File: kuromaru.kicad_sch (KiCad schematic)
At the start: 113 parts, among them J1 USB_C_Receptacle_USB2.0, J102 Serial, J5 Conn_01x02, SW1 SW_Push, SW101 SW_Push, SW102 SW_Push, SW103 SW_Push, SW104 SW_Push, SW105 SW_Push, SW106 SW_Push, SW107 SW_Push, SW108 SW_Push, SW109 SW_Push, SW110 SW_SPST, SW112 SW_Push, SW113 SW_Push, SW114 SW_Push, SW115 SW_Push, SW116 SW_Push, SW117 SW_Push, SW118 SW_Push, SW119 SW_Push, SW2 SW_Push, U1 RP2040, U2 GD25Q80CEIGR, U3 XC6210B332MR-G, Y1 Crystal_GND24

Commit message: Before diodeless design
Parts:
- removed D101, D102, D103, D104, D105, D106, D107, D108, D109, D110, D111, D112, D113, D114, D115, D116, D117: D, local-libraries:D_1206_handsolder_reversible, symbol Device:D
- removed SW101, SW102, SW103, SW104, SW105, SW106, SW107, SW108, SW109, SW112, SW113, SW114, SW115, SW116, SW117, SW118, SW119: SW_Push, local-libraries:SW_MX_choc, symbol Switch:SW_Push
- added C?: C, Capacitor_SMD:C_1206_3216Metric_Pad1.42x1.75mm_HandSolder, symbol Device:C
- added R?: R, Resistor_SMD:R_1206_3216Metric_Pad1.42x1.75mm_HandSolder, symbol Device:R
- SW1, SW2: symbol Switch:SW_Push -> delay_SW_MX_RGB:SW_Push_SK6812
- SW11, SW12, SW13, SW14, SW15, SW21, SW22, SW23, SW24, SW25, SW31, SW32, SW33, SW34, SW35, SW41, SW42: renamed from SW?; value SW_Push -> SW_Push_SK6812; symbol Switch:SW_Push -> delay_SW_MX_RGB:SW_Push_SK6812
- gave numbers to parts that had none: 5
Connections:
- net Din: now also R?.1
- net GND: no longer SW1.1, SW2.1
- net Gnd: now also SW11.3 (GND), SW11.5, SW12.3 (GND), SW12.5, SW13.3 (GND), SW13.5, SW14.3 (GND), SW14.5, SW15.3 (GND), SW15.5, SW21.3 (GND), SW21.5, SW22.3 (GND), SW22.5, SW23.3 (GND), SW23.5, SW24.3 (GND), SW24.5, SW25.3 (GND), SW25.5, SW31.3 (GND), SW31.5, SW32.3 (GND), SW32.5, SW33.3 (GND), SW33.5, SW34.3 (GND), SW34.5, SW35.3 (GND), SW35.5, SW41.3 (GND), SW41.5, SW42.3 (GND), SW42.5, C?.2; no longer SW11.1, SW12.1, SW13.1, SW14.1, SW15.1, SW21.1, SW22.1, SW23.1, SW24.1, SW25.1, SW31.1, SW32.1, SW33.1, SW34.1, SW35.1, SW41.1, SW42.1
- net Rst_l: no longer SW1.2
- net Vcc: now also SW11.1 (VDD), SW12.1 (VDD), SW13.1 (VDD), SW14.1 (VDD), SW15.1 (VDD), SW21.1 (VDD), SW22.1 (VDD), SW23.1 (VDD), SW24.1 (VDD), SW25.1 (VDD), SW31.1 (VDD), SW32.1 (VDD), SW33.1 (VDD), SW34.1 (VDD), SW35.1 (VDD), SW41.1 (VDD), SW42.1 (VDD), C?.1
- net switch11: now also SW11.6; no longer SW11.2, SW21.2, SW31.2
- net switch12: now also SW12.6; no longer SW12.2, SW22.2, SW32.2
- net switch13: now also SW13.6; no longer SW13.2, SW23.2, SW33.2
- net switch14: now also SW14.6; no longer SW14.2, SW24.2, SW34.2, SW41.2
- net switch15: now also SW15.6; no longer SW15.2, SW25.2, SW35.2, SW42.2
- net switch21: now also SW21.6
- net switch22: now also SW22.6
- net switch23: now also SW23.6
- net switch24: now also SW24.6
- net switch25: now also SW25.6
- net at J5.2 (Pin_2), R3.1: no longer SW2.2
- new net switch31: SW31.6
- new net switch32: SW32.6
- new net switch33: SW33.6
- new net switch34: SW34.6
- new net switch35: SW35.6
- new net switch41: SW41.6
- new net switch42: SW42.6
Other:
- note added: "RGB backlight"
- note added: "Switches & RGB Backlight"
- note removed: "Diodes and switches - plate"
- note removed: "Diodes and switches - thumb cluster"
- note removed: "RGB backlight - plate"

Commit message: Update to diodeless
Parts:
- removed C? (x2): C, Capacitor_SMD:C_1206_3216Metric_Pad1.42x1.75mm_HandSolder, symbol Device:C
- removed D11, D12, D13, D14, D15, D? (x12): SK6812MINI, libs2:YS-SK6812MINI-E_REVERSE, symbol LED:SK6812MINI
- removed JP111, JP112: Jumper_2_Open, local-libraries:SolderJumper-2_P1.3mm_Open_RoundedPad1.0x1.5mm, symbol Jumper:Jumper_2_Open
- removed R?: R, Resistor_SMD:R_1206_3216Metric_Pad1.42x1.75mm_HandSolder, symbol Device:R
- J102: footprint local-libraries:Jack_3.5mm_PJ320E_Horizontal_custom -> keebio:TRRS-PJ-320A-no-Fmask
- SW11: renamed from SW15; footprint local-libraries:SW_MX_choc -> local-libraries:delay_SW_MX_RGB
- SW12: renamed from SW25; footprint local-libraries:SW_MX_choc -> local-libraries:delay_SW_MX_RGB
- SW13: renamed from SW35; footprint local-libraries:SW_MX_choc -> local-libraries:delay_SW_MX_RGB
- SW14: renamed from SW42; footprint local-libraries:SW_MX_choc -> local-libraries:delay_SW_MX_RGB
- SW21: renamed from SW14; footprint local-libraries:SW_MX_choc -> local-libraries:delay_SW_MX_RGB
- SW22: renamed from SW24; footprint local-libraries:SW_MX_choc -> local-libraries:delay_SW_MX_RGB
- SW23: renamed from SW34; footprint local-libraries:SW_MX_choc -> local-libraries:delay_SW_MX_RGB
- SW24: renamed from SW41; footprint local-libraries:SW_MX_choc -> local-libraries:delay_SW_MX_RGB
- SW31: renamed from SW13; footprint local-libraries:SW_MX_choc -> local-libraries:delay_SW_MX_RGB
- SW32: renamed from SW23; footprint local-libraries:SW_MX_choc -> local-libraries:delay_SW_MX_RGB
- SW33: footprint local-libraries:SW_MX_choc -> local-libraries:delay_SW_MX_RGB
- SW41: renamed from SW12; footprint local-libraries:SW_MX_choc -> local-libraries:delay_SW_MX_RGB
- SW42: renamed from SW22; footprint local-libraries:SW_MX_choc -> local-libraries:delay_SW_MX_RGB
- SW43: renamed from SW32; footprint local-libraries:SW_MX_choc -> local-libraries:delay_SW_MX_RGB
- SW51: renamed from SW11; footprint local-libraries:SW_MX_choc -> local-libraries:delay_SW_MX_RGB
- SW52: renamed from SW21; footprint local-libraries:SW_MX_choc -> local-libraries:delay_SW_MX_RGB
- SW53: renamed from SW31; footprint local-libraries:SW_MX_choc -> local-libraries:delay_SW_MX_RGB
- gave numbers to parts that had none: 2
- renumbered SW110 to SW00
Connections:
- net Gnd is gone; now on net GND: C101.2, SW11.3 (GND), SW11.5, SW12.3 (GND), SW12.5, SW13.3 (GND), SW13.5, SW14.3 (GND), SW14.5, SW21.3 (GND), SW21.5, SW22.3 (GND), SW22.5, SW23.3 (GND), SW23.5, SW24.3 (GND), SW24.5, SW31.3 (GND), SW31.5, SW32.3 (GND), SW32.5, SW33.3 (GND), SW33.5, SW41.3 (GND), SW41.5, SW42.3 (GND), SW42.5, SW43.3 (GND), SW43.5, SW51.3 (GND), SW51.5, SW52.3 (GND), SW52.5, SW53.3 (GND), SW53.5
- net Vcc is gone; now on net +5V: C101.1, SW11.1 (VDD), SW12.1 (VDD), SW13.1 (VDD), SW14.1 (VDD), SW21.1 (VDD), SW22.1 (VDD), SW23.1 (VDD), SW24.1 (VDD), SW31.1 (VDD), SW32.1 (VDD), SW33.1 (VDD), SW41.1 (VDD), SW42.1 (VDD), SW43.1 (VDD), SW51.1 (VDD), SW52.1 (VDD), SW53.1 (VDD)
- net switch34 is gone; now on net switch23: SW23.6
- net switch35 is gone; now on net switch13: SW13.6
- net Gnd_l: now also J102.S; no longer J102.R1
- net serial_tx: now also J102.R1; no longer J102.S
- net switch11: now also SW11.6; no longer SW51.6
- net switch12: now also SW12.6; no longer SW41.6
- net switch13: no longer SW31.6
- net switch14: now also SW14.6; no longer SW21.6
- net switch15: no longer SW11.6
- net switch21: now also SW21.6; no longer SW52.6
- net switch22: now also SW22.6; no longer SW42.6
- net switch23: no longer SW32.6
- net switch24: now also SW24.6; no longer SW22.6
- net switch25: no longer SW12.6
- net switch31: now also SW31.6; no longer SW53.6
- net switch32: now also SW32.6; no longer SW43.6
- net switch41: now also SW41.6; no longer SW24.6
- net switch42: now also SW42.6; no longer SW14.6
- net at SW12.2 (DOUT): now also SW53.4 (DIN)
- net at SW12.4 (DIN): now also SW22.2 (DOUT)
- net at SW52.2 (DOUT): now also SW42.4 (DIN)
- net at SW52.4 (DIN): now also SW11.2 (DOUT)
- net at SW41.2 (DOUT): now also SW31.4 (DIN)
- net at SW41.4 (DIN): now also SW51.2 (DOUT)
- net at SW42.2 (DOUT): now also SW32.4 (DIN)
- net at SW24.2 (DOUT): now also SW14.4 (DIN)
- net at SW24.4 (DIN): now also SW13.2 (DOUT)
- net at SW13.4 (DIN): now also SW23.2 (DOUT)
- net at SW22.4 (DIN): now also SW32.2 (DOUT)
- net at SW33.2 (DOUT): now also SW23.4 (DIN)
- net at SW33.4 (DIN): now also SW43.2 (DOUT)
- net at SW43.4 (DIN): now also SW53.2 (DOUT)
- net at SW31.2 (DOUT): now also SW21.4 (DIN)
- net at R102.2: now also SW51.4 (DIN)
- net at SW11.4 (DIN): now also SW21.2 (DOUT)
- new net switch43: SW43.6
- new net switch51: SW51.6
- new net switch52: SW52.6
- new net switch53: SW53.6
- no-connect marks 10 -> 11
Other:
- note removed: "RGB backlight"
- moved on the sheet: C101, R102, SW11, SW12, SW13, SW14, SW21, SW22, SW23, SW24, SW31, SW32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

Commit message: Rework controller, commit before splay
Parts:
- removed SW00: SW_SPST, local-libraries:SW_Push_1P1T_NO_6x6mm_H9.5mm, symbol Switch:SW_SPST
- added R12, R13: 100k, Resistor_SMD:R_0402_1005Metric, symbol Device:R
- added R16, R17: 5.1k, Resistor_SMD:R_0402_1005Metric, symbol Device:R
- added U4: 25LCxxx, Package_SO:SOIC-8_3.9x4.9mm_P1.27mm, symbol Memory_EEPROM:25LCxxx
- C15: renamed from C101; value C -> 1µ; footprint Capacitor_SMD:C_1206_3216Metric_Pad1.42x1.75mm_HandSolder -> Capacitor_SMD:C_0402_1005Metric
- J102: footprint keebio:TRRS-PJ-320A-no-Fmask -> local-libraries:delay_TRRS_PJ_320A
- R15: renamed from R102; value R -> 300; footprint Resistor_SMD:R_1206_3216Metric_Pad1.42x1.75mm_HandSolder -> Resistor_SMD:R_0402_1005Metric
- SW1, SW2: symbol delay_SW_MX_RGB:SW_Push_SK6812 -> Switch:SW_Push
- renumbered SW11 to C1R1, SW12 to C1R2, SW13 to C1R3, SW14 to C1R4, SW21 to C2R1, SW22 to C2R2, SW23 to C2R3, SW24 to C2R4, SW31 to C3R1, SW32 to C3R2, SW33 to C3R3, SW41 to C4R1, SW42 to C4R2, SW43 to C4R3, SW51 to C5R1, SW52 to C5R2, SW53 to C5R3, R101 to R14
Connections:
- net Din is gone; now on net rgb_din: R15.1
- net Gnd_l is gone; now on net GND: J102.S
- net Rst_l is gone; now on net reset: R2.1, U1.26 (RUN/~{RST})
- net hand is gone; now on net hands: R14.1
- net switch42 is gone; now on net switch_c4r2: C4R2.6
- net +3V3: now also C15.1, C1R1.1 (VDD), C1R2.1 (VDD), C1R3.1 (VDD), C1R4.1 (VDD), C2R1.1 (VDD), C2R2.1 (VDD), C2R3.1 (VDD), C2R4.1 (VDD), C3R1.1 (VDD), C3R2.1 (VDD), C3R3.1 (VDD), C4R1.1 (VDD), C4R2.1 (VDD), C4R3.1 (VDD), C5R1.1 (VDD), C5R2.1 (VDD), C5R3.1 (VDD), R12.2, R16.2, R17.2, U4.8 (VCC); no longer J102.T
- net +5V: no longer C15.1, C1R1.1 (VDD), C1R2.1 (VDD), C1R3.1 (VDD), C1R4.1 (VDD), C2R1.1 (VDD), C2R2.1 (VDD), C2R3.1 (VDD), C2R4.1 (VDD), C3R1.1 (VDD), C3R2.1 (VDD), C3R3.1 (VDD), C4R1.1 (VDD), C4R2.1 (VDD), C4R3.1 (VDD), C5R1.1 (VDD), C5R2.1 (VDD), C5R3.1 (VDD)
- net GND: now also R14.2, SW1.1, SW2.1, R13.1, U4.4 (GND)
- net MISO: now also U4.2 (MISO)
- net MOSI: now also U4.5 (MOSI)
- net SCLK: now also R13.2, U4.6 (SCK)
- net VBUS: now also J102.T
- net serial_rx: now also U1.37 (GPIO25); no longer U1.4 (GPIO2)
- net serial_tx: now also U1.36 (GPIO24); no longer U1.3 (GPIO1)
- net at J5.2 (Pin_2), R3.1: now also SW2.2
- net reset: now reaches SW1.2
- net A3 renamed hands
- net D21 renamed EEPROM_CS
- net EEPROM_CS: now also R12.1, U4.1 (~{CS})
- net switch11 renamed switch_c1r1
- net switch_c1r1: now also U1.3 (GPIO1); no longer U1.5 (GPIO3)
- net switch12 renamed switch_c1r2
- net switch_c1r2: now also U1.13 (GPIO10); no longer U1.6 (GPIO4)
- net switch13 renamed switch_c1r3
- net switch_c1r3: now also U1.18 (GPIO15); no longer U1.7 (GPIO5)
- net switch14 renamed switch_c1r4
- net switch_c1r4: now also U1.29 (GPIO18); no longer U1.8 (GPIO6)
- net switch15 renamed switch_c4r2
- removed net switch21: C2R1.6, U1.11 (GPIO8), U1.16 (GPIO13)
- net switch22 renamed switch_c2r2
- net switch_c2r2: no longer U1.17 (GPIO14)
- removed net switch23: C2R3.6, U1.13 (GPIO10), U1.18 (GPIO15)
- net switch24 renamed switch_c2r4
- net switch_c2r4: no longer U1.14 (GPIO11), U1.36 (GPIO24)
- removed net switch25: U1.15 (GPIO12), U1.29 (GPIO18), U1.37 (GPIO25)
- net switch31 renamed switch_c3r1
- net switch_c3r1: now also U1.5 (GPIO3)
- net switch32 renamed switch_c3r2
- net switch_c3r2: now also U1.11 (GPIO8)
- net switch33 renamed switch_c3r3
- net switch_c3r3: now also U1.16 (GPIO13)
- net switch41 renamed switch_c4r1
- net switch_c4r1: now also U1.6 (GPIO4)
- net switch43 renamed switch_c4r3
- net switch_c4r3: now also U1.15 (GPIO12)
- net switch51 renamed switch_c5r1
- net switch_c5r1: now also U1.7 (GPIO5)
- net switch52 renamed switch_c5r2
- net switch_c5r2: now also U1.8 (GPIO6)
- net switch53 renamed switch_c5r3
- net switch_c5r3: now also U1.14 (GPIO11)
- new net: R17.1, U4.3 (~{WP})
- new net: R16.1, U4.7 (~{HOLD})
- new net switch_c2r1: C2R1.6, U1.4 (GPIO2)
- new net switch_c2r3: C2R3.6, U1.17 (GPIO14)
- no-connect marks 11 -> 6
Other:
- note added: "EEPROM"
- note added: "MCU IO assignments"
- note removed: "Board IO headers"
- note removed: "Reset button"
- moved on the sheet: C1, C10, C11, C12, C13, C14, C15, C1R1, C1R2, C1R3, C1R4, C2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

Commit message: Before messing around with orientation
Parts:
- renumbered C3R3 to C1R1, C2R3 to C1R2, C4R3 to C2R1, C5R3 to C2R2, C1R2 to C2R3, C4R2 to C3R1, C2R2 to C3R3, C5R2 to C4R1, C1R1 to C4R2, C2R1 to C4R3, C4R1 to C5R2, C3R1 to C5R3
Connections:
- net switch_c1r1: now also C1R1.6; no longer C4R2.6
- net switch_c1r2: now also C1R2.6, U1.12 (GPIO9); no longer C2R3.6, U1.13 (GPIO10)
- net switch_c2r1: now also C2R1.6; no longer C4R3.6
- net switch_c2r2: now also C2R2.6, U1.11 (GPIO8); no longer C3R3.6, U1.12 (GPIO9)
- net switch_c2r3: now also C2R3.6; no longer C1R2.6
- net switch_c3r1: now also C3R1.6; no longer C5R3.6
- net switch_c3r2: now also U1.9 (GPIO7); no longer U1.11 (GPIO8)
- net switch_c3r3: now also C3R3.6; no longer C1R1.6
- net switch_c4r1: now also C4R1.6; no longer C5R2.6
- net switch_c4r2: now also C4R2.6, U1.8 (GPIO6); no longer C3R1.6, U1.9 (GPIO7)
- net switch_c4r3: now also C4R3.6; no longer C2R1.6
- net switch_c5r2: now also C5R2.6, U1.13 (GPIO10); no longer C4R1.6, U1.8 (GPIO6)
- net switch_c5r3: now also C5R3.6; no longer C2R2.6

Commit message: Fix serial connector
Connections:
- net GND: now also J102.T; no longer J102.S
- net VBUS: now also J102.S; no longer J102.T
- net serial_rx: now also J102.R1; no longer J102.R2
- net serial_tx: now also J102.R2; no longer J102.R1

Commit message: Remove RGB
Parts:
- removed C15: 1µ, Capacitor_SMD:C_0402_1005Metric, symbol Device:C
- removed R15: 300, Resistor_SMD:R_0402_1005Metric, symbol Device:R
- C1R1, C1R2, C1R3, C1R4, C2R1, C2R2, C2R4, C3R1, C3R2, C3R3, C4R1, C4R2, C4R3, C5R2, C5R3: footprint local-libraries:delay_SW_MX_RGB -> (none); symbol delay_SW_MX_RGB:SW_Push_SK6812 -> Switch:SW_Push
- C2R3, C5R1: value SW_Push_SK6812 -> (none); footprint local-libraries:delay_SW_MX_RGB -> (none); symbol delay_SW_MX_RGB:SW_Push_SK6812 -> Switch:SW_Push
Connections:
- net rgb_din is gone; now on net switch_c1r1: U1.2 (GPIO0)
- net +3V3: no longer C1R1.1 (VDD), C1R2.1 (VDD), C1R3.1 (VDD), C1R4.1 (VDD), C2R1.1 (VDD), C2R2.1 (VDD), C2R3.1 (VDD), C2R4.1 (VDD), C3R1.1 (VDD), C3R2.1 (VDD), C3R3.1 (VDD), C4R1.1 (VDD), C4R2.1 (VDD), C4R3.1 (VDD), C5R1.1 (VDD), C5R2.1 (VDD), C5R3.1 (VDD)
- net GND: now also C1R1.1, C1R2.1, C1R3.1, C1R4.1, C2R1.1, C2R2.1, C2R3.1, C2R4.1, C3R1.1, C3R2.1, C3R3.1, C4R1.1, C4R2.1, C4R3.1, C5R1.1, C5R2.1, C5R3.1; no longer C1R1.3 (GND), C1R1.5, C1R2.3 (GND), C1R2.5, C1R3.3 (GND), C1R3.5, C1R4.3 (GND), C1R4.5, C2R1.3 (GND), C2R1.5, C2R2.3 (GND), C2R2.5, C2R3.3 (GND), C2R3.5, C2R4.3 (GND), C2R4.5, C3R1.3 (GND), C3R1.5, C3R2.3 (GND), C3R2.5, C3R3.3 (GND), C3R3.5, C4R1.3 (GND), C4R1.5, C4R2.3 (GND), C4R2.5, C4R3.3 (GND), C4R3.5, C5R1.3 (GND), C5R1.5, C5R2.3 (GND), C5R2.5, C5R3.3 (GND), C5R3.5
- net switch_c1r1: now also C1R1.2; no longer C1R1.6, U1.3 (GPIO1)
- net switch_c1r2: now also C1R2.2, U1.11 (GPIO8); no longer C1R2.6, U1.12 (GPIO9)
- net switch_c1r4: now also C1R4.2; no longer C1R4.6
- net switch_c2r1: now also C2R1.2, U1.3 (GPIO1); no longer C2R1.6, U1.4 (GPIO2)
- net switch_c2r2: now also C2R2.2, U1.9 (GPIO7); no longer C2R2.6, U1.11 (GPIO8)
- net switch_c2r3: now also C2R3.2, U1.16 (GPIO13); no longer C2R3.6, U1.17 (GPIO14)
- net switch_c2r4: now also C2R4.2; no longer C2R4.6
- net switch_c3r1: now also C3R1.2, U1.4 (GPIO2); no longer C3R1.6, U1.5 (GPIO3)
- net switch_c3r2: now also C3R2.2, U1.8 (GPIO6); no longer C3R2.6, U1.9 (GPIO7)
- net switch_c3r3: now also C3R3.2, U1.15 (GPIO12); no longer C3R3.6, U1.16 (GPIO13)
- net switch_c4r1: now also C4R1.2, U1.5 (GPIO3); no longer C4R1.6, U1.6 (GPIO4)
- net switch_c4r2: now also C4R2.2, U1.7 (GPIO5); no longer C4R2.6, U1.8 (GPIO6)
- net switch_c4r3: now also C4R3.2, U1.14 (GPIO11); no longer C4R3.6, U1.15 (GPIO12)
- net switch_c5r1: now also C5R1.2, U1.6 (GPIO4); no longer C5R1.6, U1.7 (GPIO5)
- net switch_c5r2: now also C5R2.2, U1.12 (GPIO9); no longer C5R2.6, U1.13 (GPIO10)
- net switch_c5r3: now also C5R3.2, U1.13 (GPIO10); no longer C5R3.6, U1.14 (GPIO11)
- net oled_cs: now reaches C1R3.2
- net oled_cs: now also U1.17 (GPIO14); no longer C2R4.4 (DIN)
- net switch_c1r3 renamed GPIO15
- net GPIO15: no longer C1R3.6
- no-connect marks 6 -> 5
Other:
- note added: "Switches"
- note removed: "Switches & RGB Backlight"

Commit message: Ready for order
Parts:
- removed J5: Conn_01x02, Connector_PinHeader_1.27mm:PinHeader_1x02_P1.27mm_Vertical, symbol Connector_Generic:Conn_01x02
- removed R12, R13: 100k, Resistor_SMD:R_0402_1005Metric, symbol Device:R
- removed R16, R17: 5.1k, Resistor_SMD:R_0402_1005Metric, symbol Device:R
- removed U4: 25LCxxx, Package_SO:SOIC-8_3.9x4.9mm_P1.27mm, symbol Memory_EEPROM:25LCxxx
- C1R1, C1R2, C1R3, C1R4, C2R1, C2R2, C2R4, C3R1, C3R2, C3R3, C4R1, C4R2, C4R3, C5R2, C5R3: value SW_Push_SK6812 -> (none); JLCPCB BOM (none) -> 0
- C2R3, C5R1: JLCPCB BOM (none) -> 0
- J102: value Serial -> (none); footprint local-libraries:delay_TRRS_PJ_320A -> (none); JLCPCB BOM (none) -> 0
- R14: value 5.1k -> (none); footprint local-libraries:R_0402_1005Metric_nolabel -> (none); JLCPCB Part C26033 -> (none); LCSC (none) -> C26033
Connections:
- net A2 is gone; now on net hands: U1.40 (GPIO28_ADC2)
- net hands: no longer U1.41 (GPIO29_ADC3)
- new net A3: U1.41 (GPIO29_ADC3)
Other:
- note removed: "EEPROM"

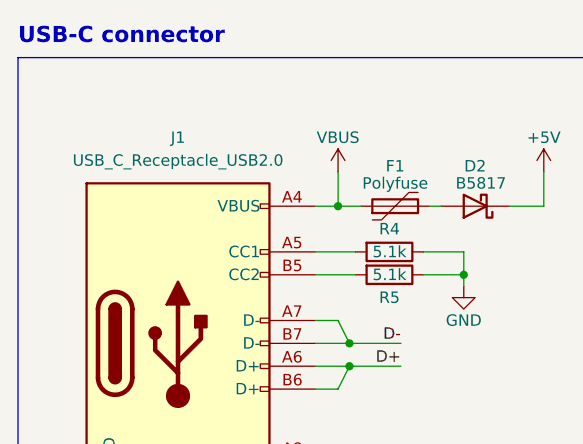
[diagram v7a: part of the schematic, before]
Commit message: Update USB-C port to use M14
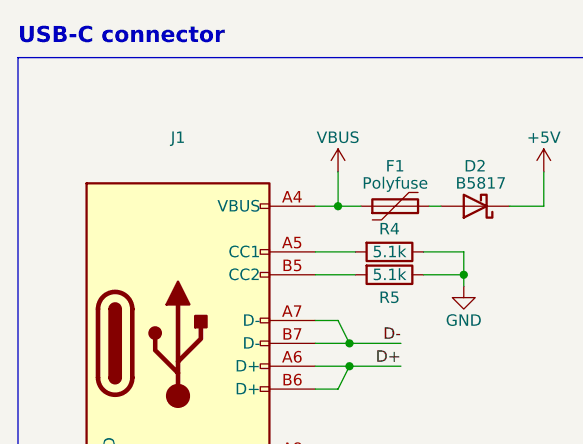
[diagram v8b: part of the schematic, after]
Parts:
- J1: value USB_C_Receptacle_USB2.0 -> (none); footprint 0xLib_USB_Type-C:USB_C_Receptacle_HRO_TYPE-C-31-M-13B -> (none); LCSC C2848619 -> C223907
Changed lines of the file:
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@@
     (in_bom yes) (on_board yes) (fields_autoplaced)
     (property "Reference" "J1" (id 0) (at 35.56 29.21 0))
-    (property "Value" "USB_C_Receptacle_USB2.0" (id 1) (at 35.56 31.75 0))
-    (property "Footprint" "0xLib_USB_Type-C:USB_C_Receptacle_HRO_TYPE-C-31-M-13B" (id 2) (at 39.37 52.07 0)
+    (property "Value" "" (id 1) (at 35.56 31.75 0))
+    (property "Footprint" "" (id 2) (at 39.37 52.07 0)
       (effects (font (size 1.27 1.27)) hide)
     )
@@
       (effects (font (size 1.27 1.27)) hide)
     )
-    (property "LCSC" "C2848619" (id 4) (at 35.56 52.07 0)
+    (property "LCSC" "C223907" (id 4) (at 35.56 52.07 0)
       (effects (font (size 1.27 1.27)) hide)
     )
